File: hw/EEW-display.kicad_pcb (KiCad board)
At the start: 2 copper layers, 139 x 64 mm, 47 parts, among them J1 USB4105-GF-A, J2 B2B-PH-K-S, Q1 SSM3J332R, SW1 PAGE/BOOT, SW2 ZOOM-IN, SW3 MODE, SW4 ZOOM-OUT, SW5 SLIDE_SW, U1 ESP32-S3-WROOM-1-N16R8, U2 MCP73831T-2ATI/OT, U3 SPX3819M5-L, U4 MAX98357A, U5 ILI9488 MCU I8080 8/16BIT 3/4, Y1 32.7680KHz

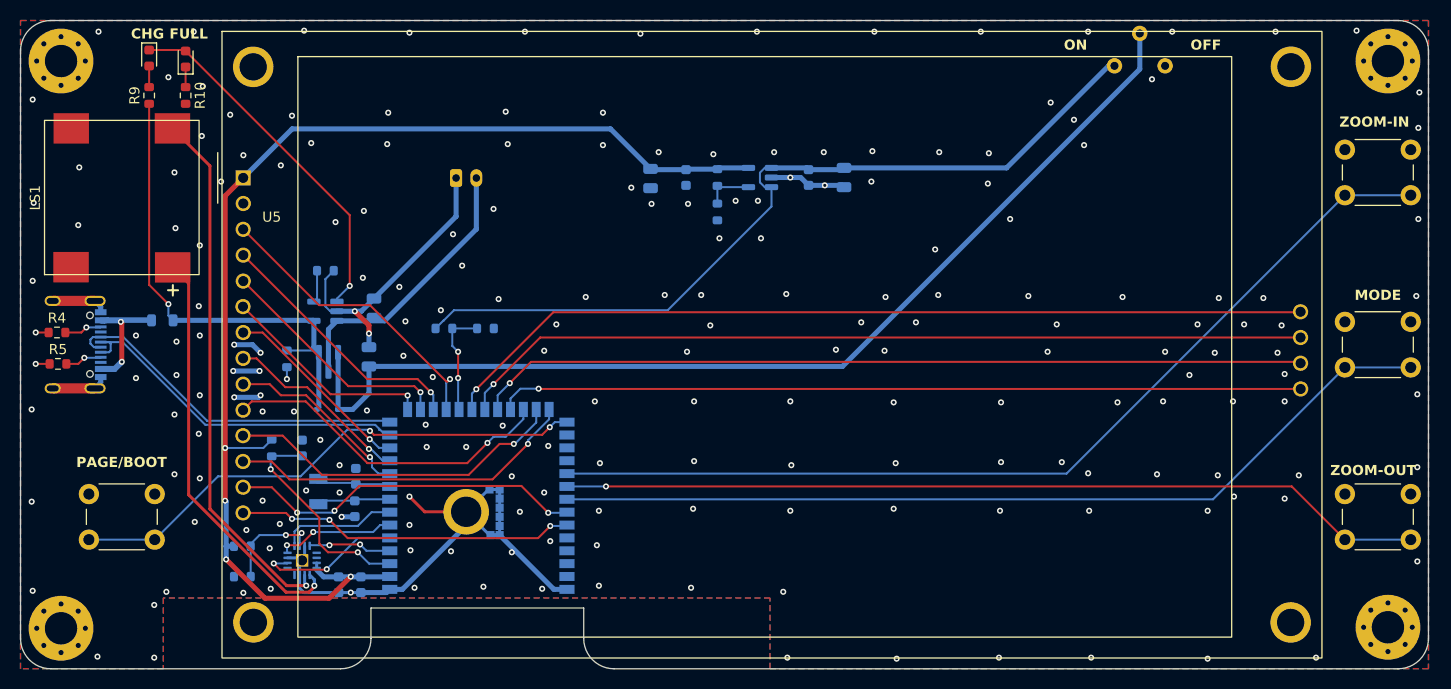
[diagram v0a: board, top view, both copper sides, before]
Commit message: Fixed Display Footprint and C1 capacitor value
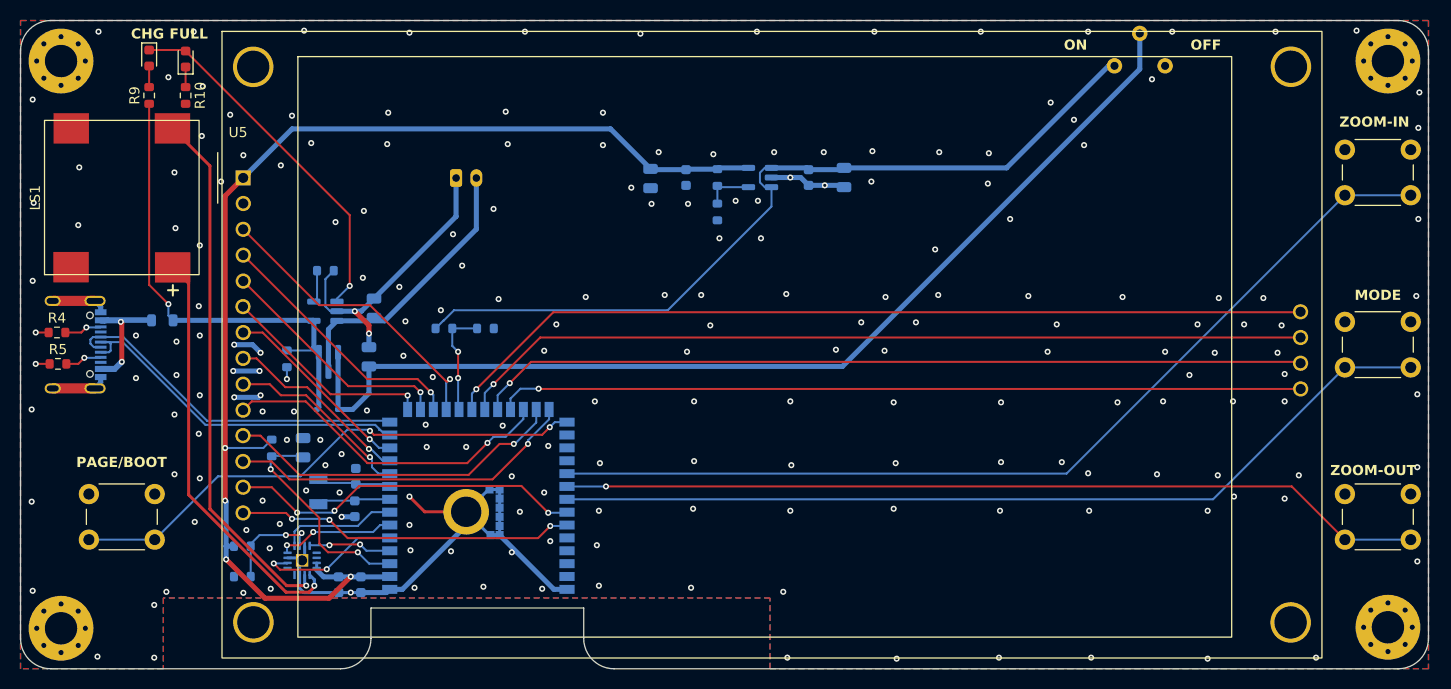
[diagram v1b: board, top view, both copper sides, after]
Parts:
- C1: value 0.1uF -> 1uF; footprint Capacitor_SMD:C_0603_1608Metric -> Capacitor_SMD:C_0805_2012Metric
- LS1: footprint tbctl:Speaker_UM1515IA -> Library:Speaker_UM1515IA
- U4: footprint tbctl:TQFN-16-1EP_3x3mm_P0.5mm_EP1.23x1.23mm -> Library:TQFN-16-1EP_3x3mm_P0.5mm_EP1.23x1.23mm
- U5: footprint tbctl:ILI9488 MCU I8080 -> Library:ILI9488 MCU I8080
- moved C1 0.10 mm to (113.9, 95.2)
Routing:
- net GND: vias 207 -> 209
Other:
- board text added: "(C) 2026 HNZ EEW-DISPLAY R2"
- board text removed: "(C) 2026 HNZ EEW-DISPLAY"
